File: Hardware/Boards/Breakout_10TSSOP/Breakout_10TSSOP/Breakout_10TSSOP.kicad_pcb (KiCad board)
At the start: 2 copper layers, 21.6 x 19 mm, 3 parts, among them J1 Conn_01x05_Male, J2 Conn_01x05_Male, U1 CS5343-CZZ

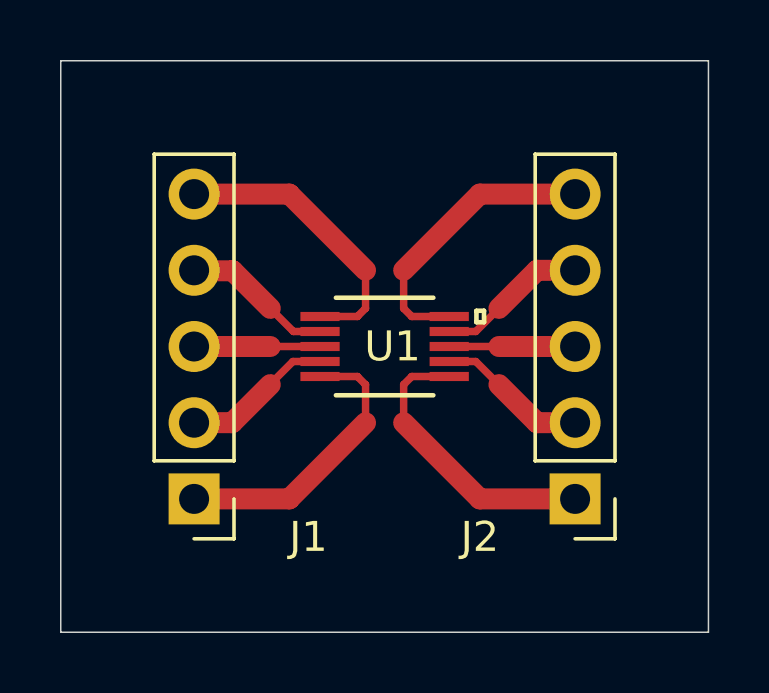
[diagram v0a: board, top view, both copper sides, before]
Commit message: Revised PCB for the 10TSSOP Breakout board. Sent in for fabrication.
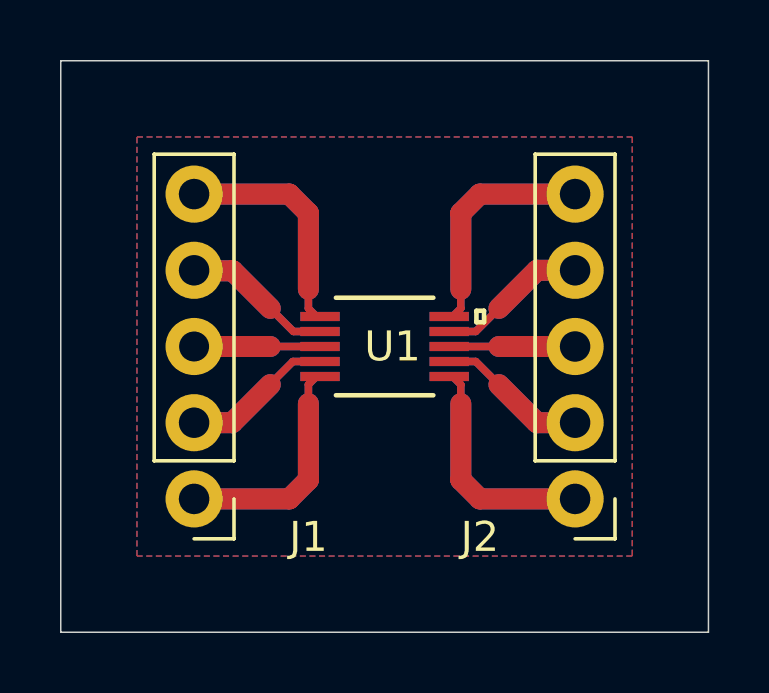
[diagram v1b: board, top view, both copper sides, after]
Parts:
- added U1: CS5343-CZZ, CS5343CZZ:CS5343-CZZ, B.Cu at (130.2, 108.0)
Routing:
- net 1: track 9.67 -> 15.7 mm
- net 10: track 9.67 -> 15.5 mm
- net 6: track 9.67 -> 15.5 mm
- net 5: track 9.67 -> 15.5 mm
- net 4: track 5.05 -> 10.1 mm
- net 9: track 5.04 -> 10.1 mm
- net 7: track 5.04 -> 10.1 mm
- net 2: track 5.04 -> 10.1 mm
- net 8: track 4.20 -> 8.39 mm
- net 3: track 4.20 -> 8.39 mm
- added copper zone on B.Cu, net (none)
- added copper zone on F.Cu, net (none)
